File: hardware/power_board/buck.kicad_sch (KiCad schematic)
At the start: 16 parts, among them U1 TPS54360DDA

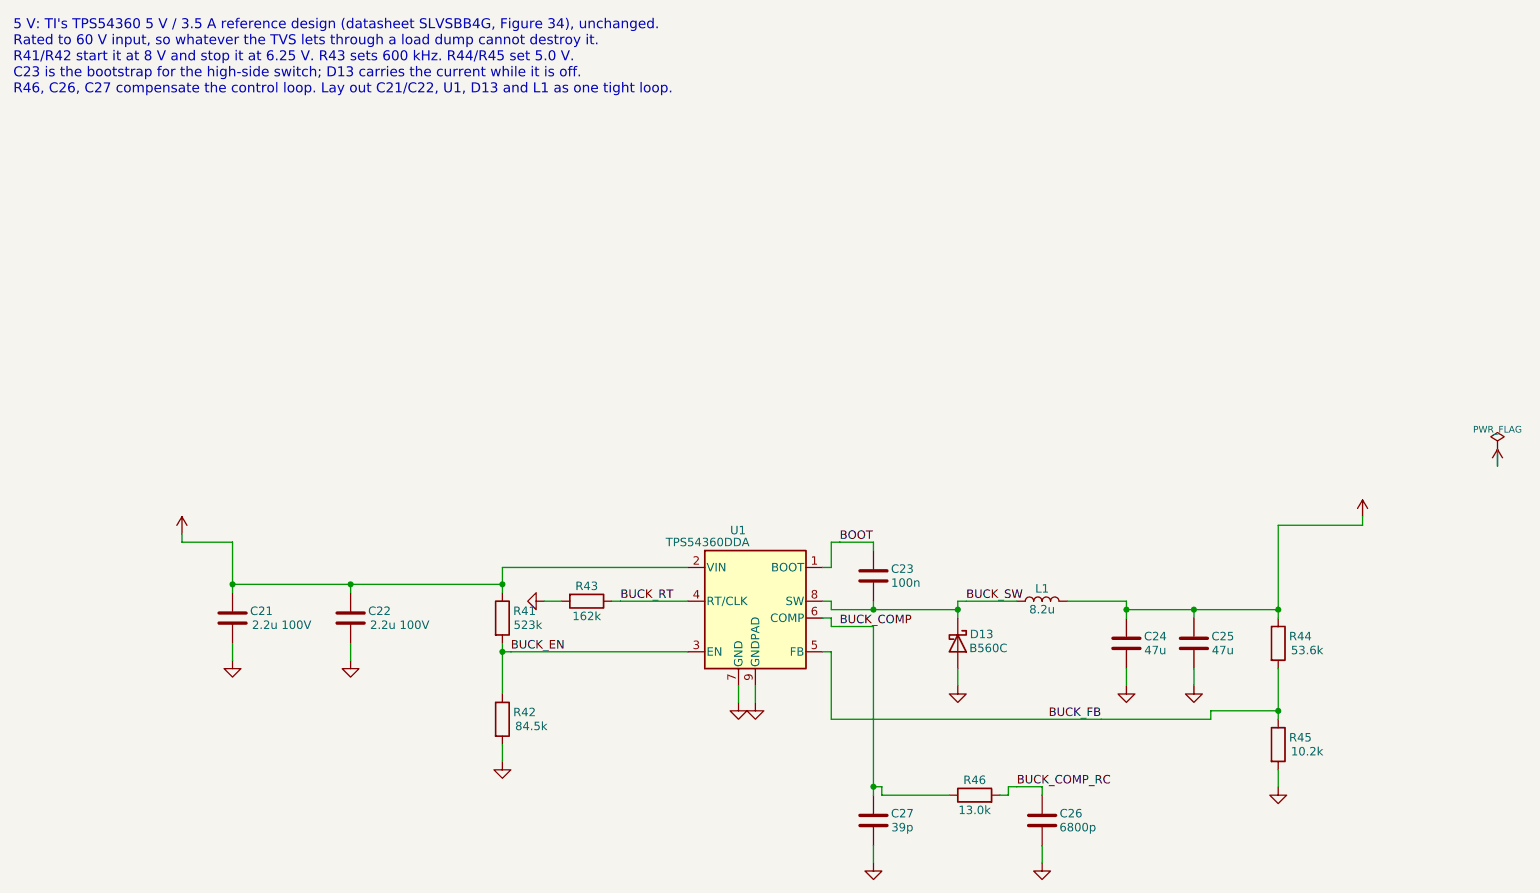
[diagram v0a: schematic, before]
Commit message: Pod board schematic redrawn as wired sheets; duplicate references fixed
pod_board_drawing.py draws six sheets around an MCU sheet under a block
diagram; check.sh now compares both boards' drawn and label-only netlists.
kisheet.py: stacked pins, PWR_FLAGs on signal nets, column hints for
crossing-free fan-ins, nets drawn in pieces joined by name, and visible
rail names on power symbols.

R31-R33 were used twice on the pod board, which KiCad's ERC does not
report; the netlist merged each pair. Cable parts now start at R40/C40,
generate.py rejects duplicate references and check_nets.py fails on a pin
in two nets. check_nets.py also drops the sheet path from net names.
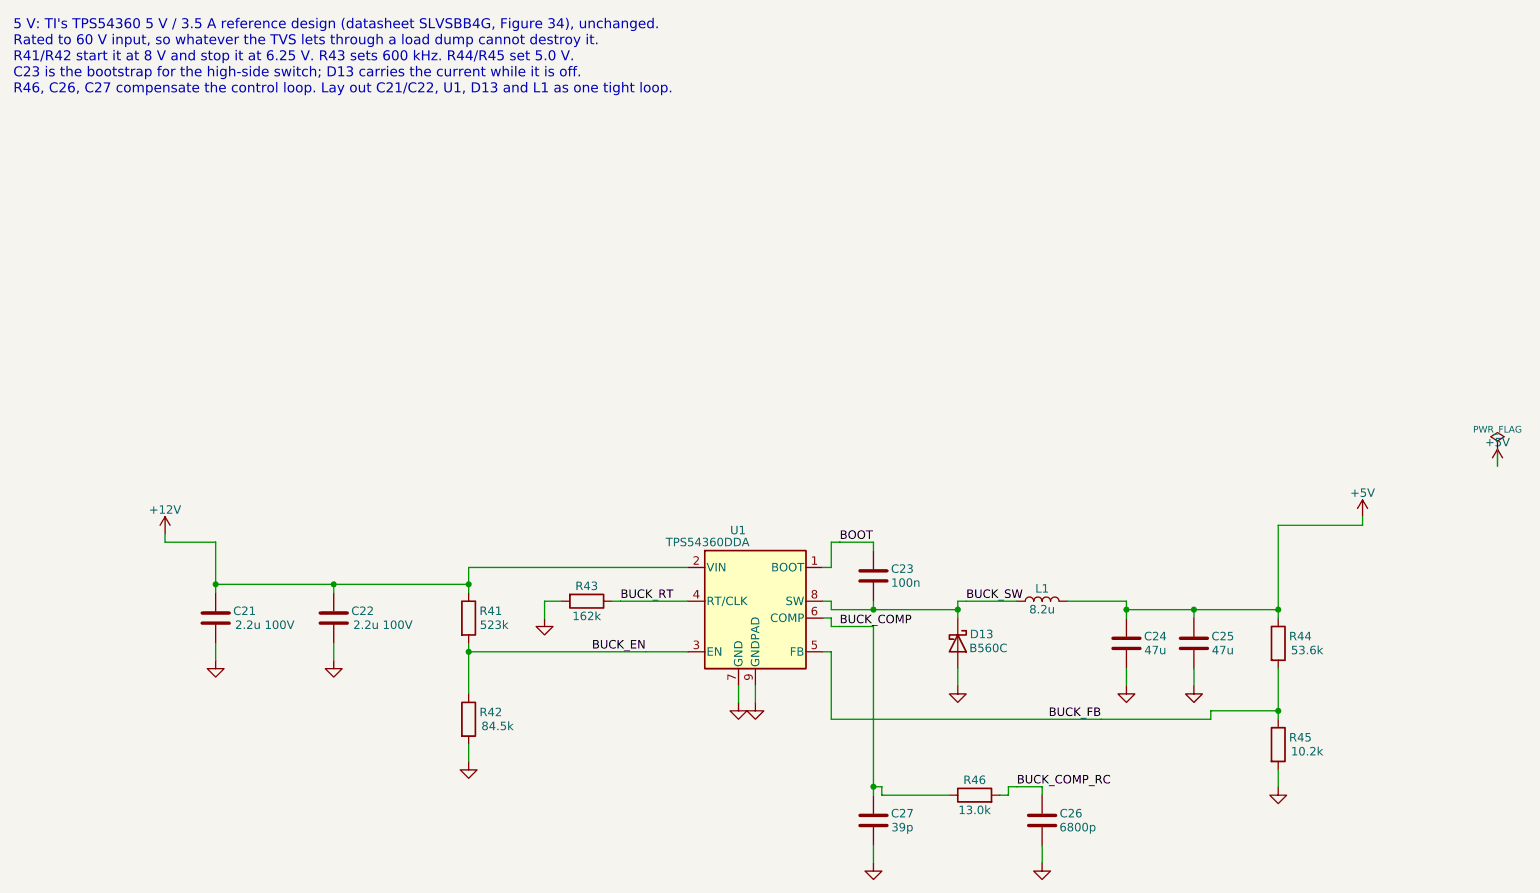
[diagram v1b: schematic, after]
